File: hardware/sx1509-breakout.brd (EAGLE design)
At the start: 25.4 x 38.1 mm, 33 parts, among them U1 SX1509

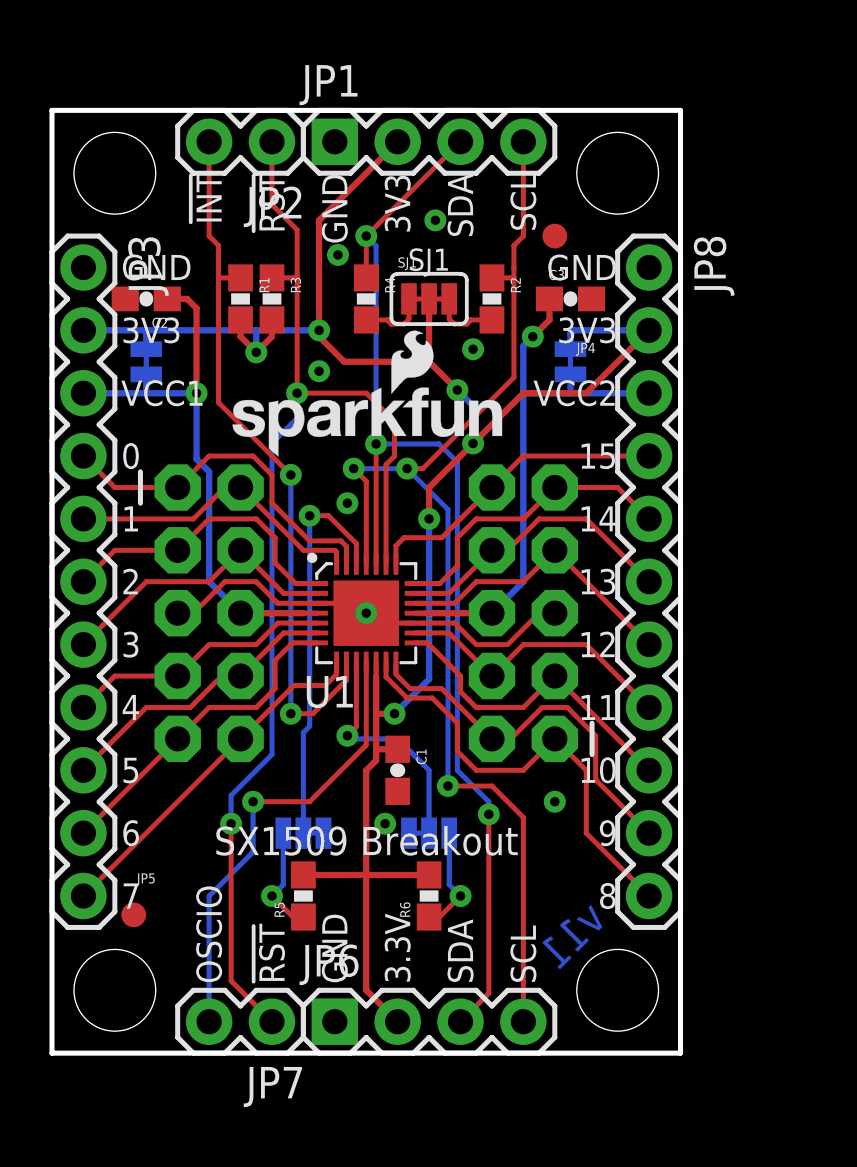
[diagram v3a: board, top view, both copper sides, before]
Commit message: Revising GPIO headers to single 2x10 header.
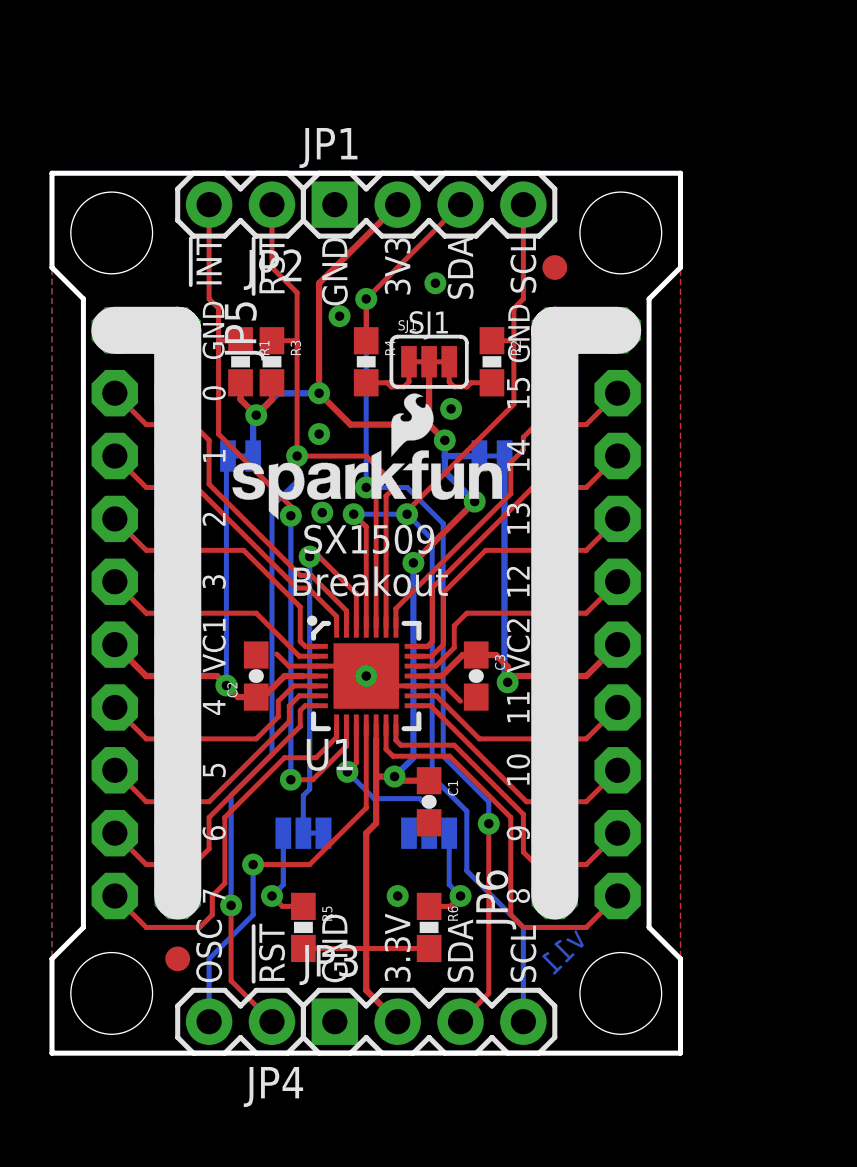
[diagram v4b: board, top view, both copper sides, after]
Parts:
- removed JP7: (no value), SparkFun-Connectors:1X02
- removed JP8: (no value), SparkFun-Connectors:1X11
- JP3: device SparkFun-Connectors:1X11 -> SparkFun-Connectors:1X04
- JP4: value IDC-5X2 -> (none); device SparkFun-Connectors:2X5-SHROUDED-NS -> SparkFun-Connectors:1X02
- JP5: value IDC-5x2 -> (none); device SparkFun-Connectors:2X5-SHROUDED-NS -> SparkFun-Connectors:2X10_NOSILK
- JP6: device SparkFun-Connectors:1X04 -> SparkFun-Connectors:2X10_NOSILK
- moved JP3 32.1 mm to (11.4, 1.27), turned to 0 degrees
- moved JP4 19.4 mm to (8.89, 1.27)
- moved JP6 19.4 mm to (21.6, 17.8), turned to 90 degrees
- moved C2 15.9 mm to (8.26, 15.2), turned to 90 degrees
- moved C3 15.7 mm to (17.1, 15.2), turned to 270 degrees
- moved LOGO3 11.1 mm to (16.1, 27.7)
- moved LOGO2 11.1 mm to (10.0, 26.3)
- moved FRAME1 9.25 mm to (-13.0, -17.8)
- moved SJ2 5.39 mm to (7.62, 24.1), turned to 180 degrees
- moved SJ3 4.96 mm to (17.8, 24.1), turned to 0 degrees
- moved U1 2.54 mm to (12.7, 15.2)
- moved JP5 2.54 mm to (3.81, 17.8), turned to 270 degrees
- moved JP1 2.54 mm to (11.4, 34.3)
- moved JP2 2.54 mm to (8.89, 34.3)
- moved LOGO1 2.54 mm to (6.86, 21.5)
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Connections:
- net !RESET: now also JP4.1; no longer JP7.1
- net 0: now also JP5.3; no longer JP3.4, JP5.1
- net 1: now also JP5.5; no longer JP3.5, JP5.2
- net 10: now also JP6.5; no longer JP4.3, JP8.9
- net 11: now also JP6.7; no longer JP4.4, JP8.8
- net 12: now also JP6.11; no longer JP4.7, JP8.7
- net 13: now also JP6.13; no longer JP4.8, JP8.6
- net 14: now also JP6.15; no longer JP4.9, JP8.5
- net 15: now also JP6.17; no longer JP4.10, JP8.4
- net 2: now also JP5.7; no longer JP3.6, JP5.3
- net 3: now also JP5.9; no longer JP3.7, JP5.4
- net 3.3V: no longer JP6.2, JP8.2
- net 4: now also JP5.13; no longer JP3.8, JP5.7
- net 5: now also JP5.15; no longer JP3.9, JP5.8
- net 6: now also JP5.17; no longer JP3.10, JP5.9
- net 7: now also JP5.19; no longer JP3.11, JP5.10
- net 8: now also JP6.1; no longer JP4.1, JP8.11
- net 9: now also JP6.3; no longer JP4.2, JP8.10
- net GND: now also JP5.1, JP5.10, JP5.12, JP5.14, JP5.16, JP5.18, JP5.2, JP5.20, JP5.4, JP5.6, JP5.8, JP6.10, JP6.12, JP6.14, JP6.16, JP6.18, JP6.19, JP6.2, JP6.20, JP6.4, JP6.6, JP6.8; no longer JP4.5, JP5.5, JP6.1, JP8.1
- net OSCIO: now also JP4.2; no longer JP7.2
- net SCL: now also JP3.4; no longer JP6.4
- net SDA: now also JP3.3; no longer JP6.3
- net VCC1: now also JP5.11; no longer JP3.3, JP5.6
- net VCC2: now also JP6.9; no longer JP4.6, JP8.3
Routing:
- net 3.3V: track 82.0 -> 62.3 mm
- net GND: track 17.8 -> 9.02 mm, vias 8 -> 7
- net VCC1: track 22.8 -> 18.7 mm
- net VCC2: track 22.6 -> 19.2 mm
- net SCL: track 48.0 -> 44.7 mm, vias 3 -> 2
- net 10: track 13.0 -> 10.3 mm
- net ADDR1: track 9.55 -> 6.97 mm
- net OSCIO: track 18.5 -> 16.0 mm
- net !RESET: track 49.1 -> 46.6 mm
- net 9: track 15.5 -> 13.1 mm
- net 3: track 11.8 -> 9.43 mm
- net 11: track 11.8 -> 9.43 mm
- net SDA: track 47.7 -> 45.6 mm
- net 8: track 18.1 -> 16.2 mm
- net 15: track 12.5 -> 14.4 mm
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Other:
- board size 25.4 x 38.1 mm -> 25.4 x 35.6 mm
- board text added: "I2C ADDR"
- board text added: "OSC"
- board text added: "Units: inches"
- board text added: "VC1"
- board text added: "VC2"
- board text removed: "I2C ADD"
- board text removed: "OSCIO"
- board text removed: "VCC1"
- board text removed: "VCC2"
